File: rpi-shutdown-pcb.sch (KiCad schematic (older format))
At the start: 14 parts

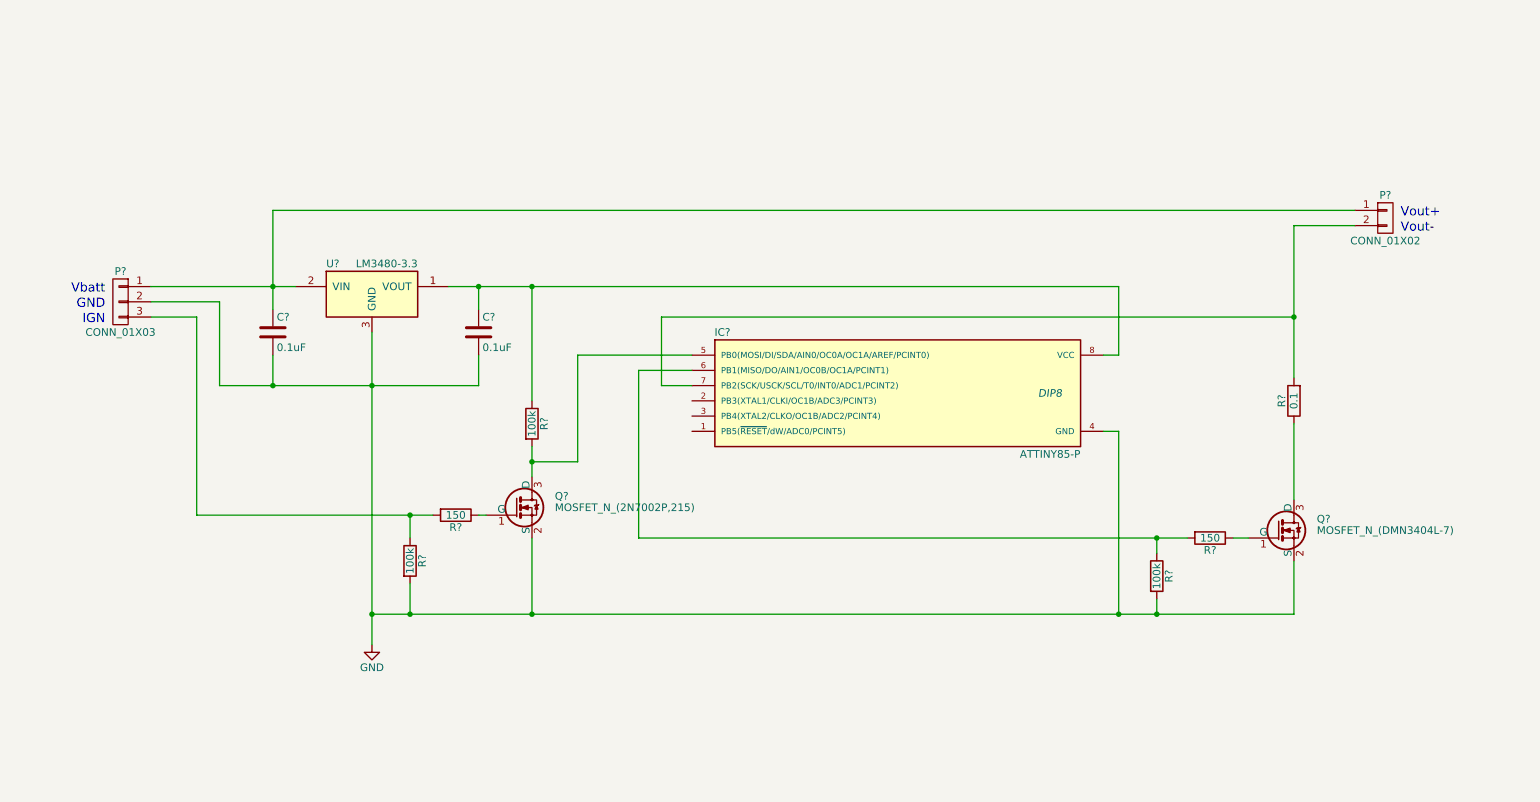
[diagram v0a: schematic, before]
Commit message: finished revised circuit with P-channel FET and footprints
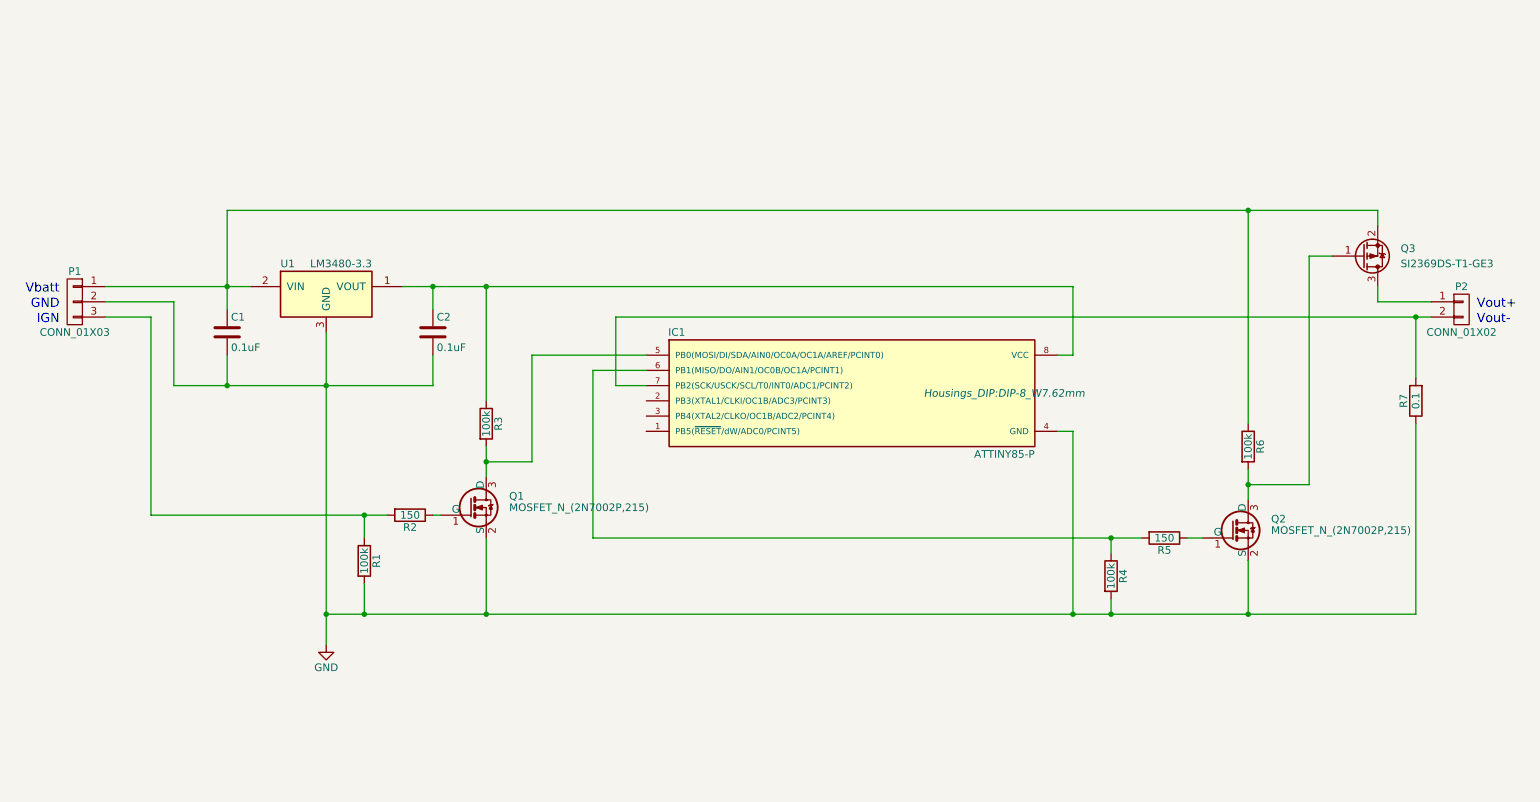
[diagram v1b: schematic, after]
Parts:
- removed Q?: MOSFET_N_(DMN3404L-7), symbol MOSFET_N_(DMN3404L-7)
- added Q2: MOSFET_N_(2N7002P,215), TO_SOT_Packages_SMD:SOT-23_Handsoldering, symbol MOSFET_N_(2N7002P,215)
- added Q3: SI2369DS-T1-GE3, TO_SOT_Packages_SMD:SOT-23_Handsoldering, symbol Q_PMOS_GSD
- added R6: 100k, Resistors_SMD:R_1206_HandSoldering, symbol R
- C1, C2: renamed from C?; footprint (none) -> Capacitors_SMD:C_1206_HandSoldering
- IC1: renamed from IC?; footprint DIP8 -> Housings_DIP:DIP-8_W7.62mm
- P1: renamed from P?; footprint (none) -> rpi-shutdown-pcb:3_PADS_FOR_18_AWG_WIRE
- P2: renamed from P?; footprint (none) -> rpi-shutdown-pcb:2_PADS_FOR_18_AWG_WIRE
- Q1: renamed from Q?; footprint (none) -> TO_SOT_Packages_SMD:SOT-23_Handsoldering
- R1, R2, R3, R4, R5, R7: renamed from R?; footprint (none) -> Resistors_SMD:R_1206_HandSoldering
- U1: renamed from U?; footprint TO_SOT_Packages_SMD:SOT-23 -> TO_SOT_Packages_SMD:SOT-23_Handsoldering
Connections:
- net GND: now also R7.1, Q2.2 (S)
- net at C1.1, P1.1 (P1), U1.2 (VIN): now also Q3.2 (S), R6.1; no longer P2.1 (P1)
- net at R5.1: now also Q2.1 (G)
- new net: P2.1 (P1), Q3.3 (D)
- new net: Q2.3 (D), Q3.1 (G), R6.2
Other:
- moved on the sheet: C1, C2, IC1, P1, P2, Q1, R1, R2, R3, R4, R5, R7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

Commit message: -finished pcb layout.
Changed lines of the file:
@@
 LIBS:valves
 LIBS:rpi-shutdown-pcb
-LIBS:Smart Tank Motherboard-cache
 LIBS:rpi-shutdown-pcb-cache
 EELAYER 25 0
@@
 F 0 "IC1" H 5250 4250 50  0000 C CNN
 F 1 "ATTINY85-P" H 7400 3450 50  0000 C CNN
-F 2 "Housings_DIP:DIP-8_W7.62mm" H 7400 3850 50  0000 C CIN
+F 2 "Housings_DIP:DIP-8_W7.62mm" H 7400 3850 50  0001 C CIN
 F 3 "" H 6400 3850 50  0000 C CNN
 	1    6400 3850

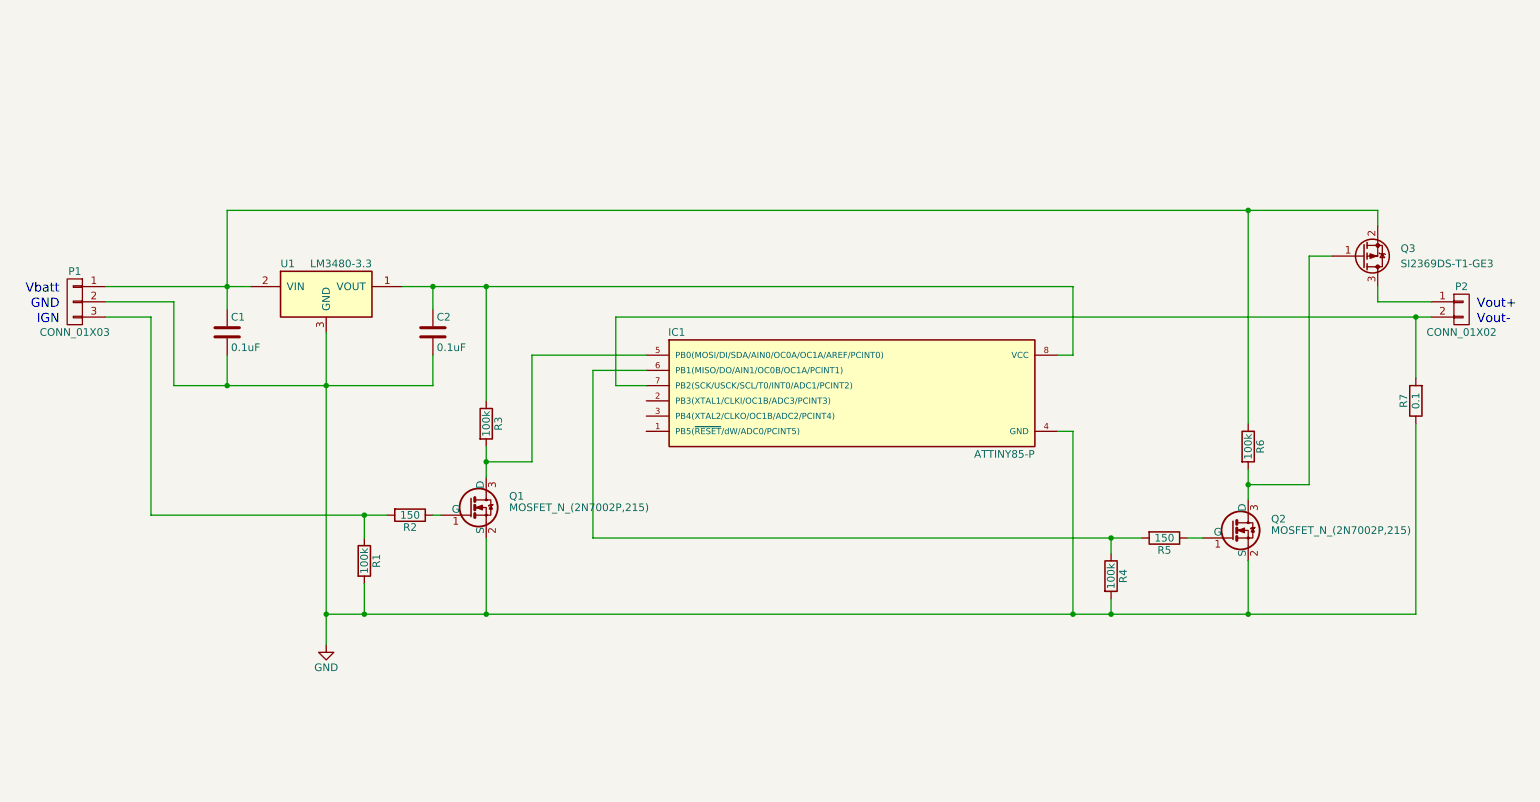
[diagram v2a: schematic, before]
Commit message: Finished adding step-down converter circuit.  Need to start on footprints.
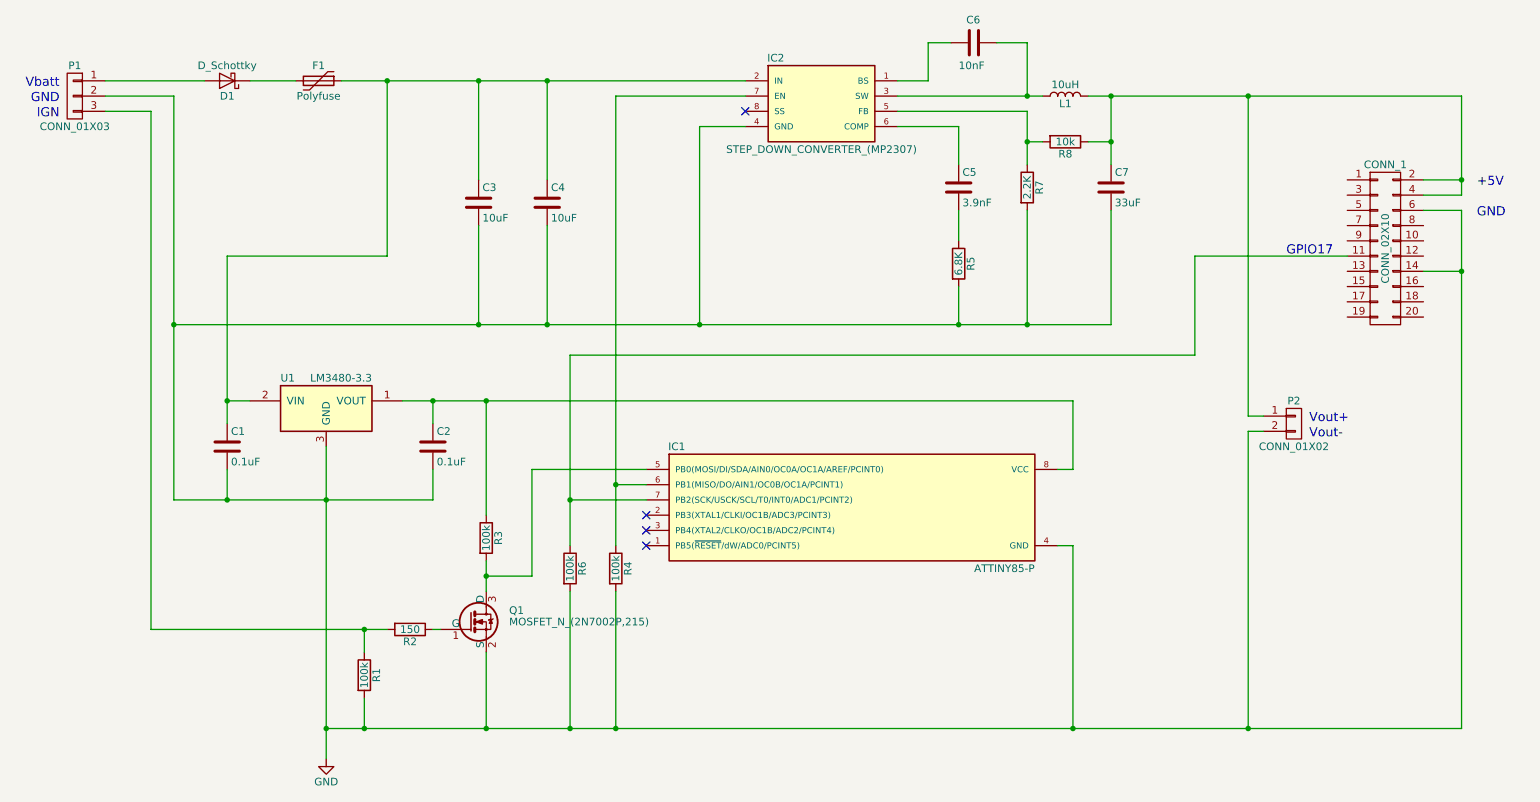
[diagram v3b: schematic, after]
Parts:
- removed Q2: MOSFET_N_(2N7002P,215), TO_SOT_Packages_SMD:SOT-23_Handsoldering, symbol MOSFET_N_(2N7002P,215)
- removed Q3: SI2369DS-T1-GE3, TO_SOT_Packages_SMD:SOT-23_Handsoldering, symbol Q_PMOS_GSD
- added C3, C4: 10uF, Capacitors_SMD:C_1206_HandSoldering, symbol C
- added C5: 3.9nF, Capacitors_SMD:C_1206_HandSoldering, symbol C
- added C6: 10nF, Capacitors_SMD:C_1206_HandSoldering, symbol C
- added C7: 33uF, Capacitors_SMD:C_1206_HandSoldering, symbol C
- added CONN_1: CONN_02X10, symbol CONN_02X10
- added D1: D_Schottky, symbol D_Schottky
- added F1: Polyfuse, symbol Polyfuse
- added IC2: STEP_DOWN_CONVERTER_(MP2307), DIP8, symbol STEP_DOWN_CONVERTER_(MP2307)
- added L1: 10uH, symbol L
- added R8: 10k, Resistors_SMD:R_1206_HandSoldering, symbol R
- P1: footprint rpi-shutdown-pcb:3_PADS_FOR_18_AWG_WIRE -> (none)
- R5: value 150 -> 6.8K
- R7: value 0.1 -> 2.2K
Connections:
- net GND: now also P2.2 (P2), R5.2, R6.2, R7.2, C3.2, C4.2, C7.2, CONN_1.14 (P14), CONN_1.6 (P6), IC2.4 (GND), IC2.9 (GND); no longer R7.1
- net at IC1.6 (PB1(MISO/DO/AIN1/OC0B/OC1A/PCINT1)), R4.1: now also IC2.7 (EN); no longer R5.2
- net at C1.1, U1.2 (VIN): now also C3.1, C4.1, F1.1, IC2.2 (IN); no longer P1.1 (P1), R6.1
- net at P2.1 (P1): now also C7.1, CONN_1.2 (P2), CONN_1.4 (P4), L1.2, R8.1
- net at R5.1: now also C5.2
- new net: CONN_1.11 (P11), IC1.7 (PB2(SCK/USCK/SCL/T0/INT0/ADC1/PCINT2)), R6.1
- new net: C6.2, IC2.1 (BS)
- new net: C6.1, IC2.3 (SW), L1.1
- new net: IC2.5 (FB), R7.1, R8.2
- new net: C5.1, IC2.6 (COMP)
- new net: D1.1 (K), F1.2
- new net: D1.2 (A), P1.1 (P1)
- no-connect marks 0 -> 4
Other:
- note added: "+5V"
- note added: "GPIO17"
- moved on the sheet: C1, C2, IC1, P2, Q1, R1, R2, R3, R6, U1

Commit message: Finished footprints.
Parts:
- C1, C2, C3, C4, C7: footprint Capacitors_SMD:C_1206_HandSoldering -> rpi-shutdown-pcb:R_1206_HandSoldering_(narrow)
- C5, C6: footprint Capacitors_SMD:C_1206_HandSoldering -> rpi-shutdown-pcb:C_0805_HandSoldering_(narrow)
- CONN_1: footprint (none) -> rpi-shutdown-pcb:HEADER_20_PIN_FEMALE_(PPTC102LFBN-RC)
- D1: footprint (none) -> rpi-shutdown-pcb:DO-214AB
- F1: footprint (none) -> rpi-shutdown-pcb:R_1812_HandSoldering
- IC2: footprint DIP8 -> rpi-shutdown-pcb:SOIC8N_(EXPOSED_PAD)
- P1: footprint (none) -> rpi-shutdown-pcb:3_PADS_FOR_18_AWG_WIRE
- R1, R2, R3, R4, R5, R6, R7, R8: footprint Resistors_SMD:R_1206_HandSoldering -> rpi-shutdown-pcb:R_1206_HandSoldering_(narrow)
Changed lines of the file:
@@
 F 0 "C1" H 2325 4300 50  0000 L CNN
 F 1 "0.1uF" H 2325 4100 50  0000 L CNN
-F 2 "Capacitors_SMD:C_1206_HandSoldering" H 2338 4050 50  0001 C CNN
+F 2 "rpi-shutdown-pcb:R_1206_HandSoldering_(narrow)" H 2338 4050 50  0001 C CNN
 F 3 "" H 2300 4200 50  0000 C CNN
 	1    2300 4200
@@
 F 0 "C2" H 3675 4300 50  0000 L CNN
 F 1 "0.1uF" H 3675 4100 50  0000 L CNN
-F 2 "Capacitors_SMD:C_1206_HandSoldering" H 3688 4050 50  0001 C CNN
+F 2 "rpi-shutdown-pcb:R_1206_HandSoldering_(narrow)" H 3688 4050 50  0001 C CNN
 F 3 "" H 3650 4200 50  0000 C CNN
 	1    3650 4200
@@
 F 0 "R2" V 3580 5400 50  0000 C CNN
 F 1 "150" V 3500 5400 50  0000 C CNN
-F 2 "Resistors_SMD:R_1206_HandSoldering" V 3430 5400 50  0001 C CNN
+F 2 "rpi-shutdown-pcb:R_1206_HandSoldering_(narrow)" V 3430 5400 50  0001 C CNN
 F 3 "" H 3500 5400 50  0000 C CNN
 	1    3500 5400
@@
 F 0 "R3" V 4080 4800 50  0000 C CNN
 F 1 "100k" V 4000 4800 50  0000 C CNN
-F 2 "Resistors_SMD:R_1206_HandSoldering" V 3930 4800 50  0001 C CNN
+F 2 "rpi-shutdown-pcb:R_1206_HandSoldering_(narrow)" V 3930 4800 50  0001 C CNN
 F 3 "" H 4000 4800 50  0000 C CNN
 	1    4000 4800
@@
 F 0 "R1" V 3280 5700 50  0000 C CNN
 F 1 "100k" V 3200 5700 50  0000 C CNN
-F 2 "Resistors_SMD:R_1206_HandSoldering" V 3130 5700 50  0001 C CNN
+F 2 "rpi-shutdown-pcb:R_1206_HandSoldering_(narrow)" V 3130 5700 50  0001 C CNN
 F 3 "" H 3200 5700 50  0000 C CNN
 	1    3200 5700
@@
 F 0 "R6" V 4630 5000 50  0000 C CNN
 F 1 "100k" V 4550 5000 50  0000 C CNN
-F 2 "Resistors_SMD:R_1206_HandSoldering" V 4480 5000 50  0001 C CNN
+F 2 "rpi-shutdown-pcb:R_1206_HandSoldering_(narrow)" V 4480 5000 50  0001 C CNN
 F 3 "" H 4550 5000 50  0000 C CNN
 	1    4550 5000
@@
 F 0 "IC2" H 5900 2250 50  0000 C CNN
 F 1 "STEP_DOWN_CONVERTER_(MP2307)" H 6200 1650 50  0000 C CNN
-F 2 "DIP8" H 6200 1550 50  0001 C CIN
+F 2 "rpi-shutdown-pcb:SOIC8N_(EXPOSED_PAD)" H 6200 1550 50  0001 C CIN
 F 3 "" H 6200 1950 50  0000 C CNN
 	1    6200 1950
@@
 F 0 "D1" H 2300 1900 50  0000 C CNN
 F 1 "D_Schottky" H 2300 1700 50  0000 C CNN
-F 2 "" H 2300 1800 50  0001 C CNN
+F 2 "rpi-shutdown-pcb:DO-214AB" H 2300 1800 50  0001 C CNN
 F 3 "" H 2300 1800 50  0001 C CNN
 	1    2300 1800
@@
 F 0 "F1" V 2800 1800 50  0000 C CNN
 F 1 "Polyfuse" V 3000 1800 50  0000 C CNN
-F 2 "" H 2950 1600 50  0001 L CNN
+F 2 "rpi-shutdown-pcb:R_1812_HandSoldering" H 2950 1600 50  0001 L CNN
 F 3 "" H 2900 1800 50  0001 C CNN
 	1    2900 1800
@@
 F 0 "C3" H 3975 2700 50  0000 L CNN
 F 1 "10uF" H 3975 2500 50  0000 L CNN
-F 2 "Capacitors_SMD:C_1206_HandSoldering" H 3988 2450 50  0001 C CNN
+F 2 "rpi-shutdown-pcb:R_1206_HandSoldering_(narrow)" H 3988 2450 50  0001 C CNN
 F 3 "" H 3950 2600 50  0000 C CNN
 	1    3950 2600
@@
 F 0 "C4" H 4425 2700 50  0000 L CNN
 F 1 "10uF" H 4425 2500 50  0000 L CNN
-F 2 "Capacitors_SMD:C_1206_HandSoldering" H 4438 2450 50  0001 C CNN
+F 2 "rpi-shutdown-pcb:R_1206_HandSoldering_(narrow)" H 4438 2450 50  0001 C CNN
 F 3 "" H 4400 2600 50  0000 C CNN
 	1    4400 2600
@@
 F 0 "C6" V 7050 1500 50  0000 L CNN
 F 1 "10nF" V 7350 1450 50  0000 L CNN
-F 2 "Capacitors_SMD:C_1206_HandSoldering" H 7238 1400 50  0001 C CNN
+F 2 "rpi-shutdown-pcb:C_0805_HandSoldering_(narrow)" H 7238 1400 50  0001 C CNN
 F 3 "" H 7200 1550 50  0000 C CNN
 	1    7200 1550
@@
 F 0 "R7" V 7630 2500 50  0000 C CNN
 F 1 "2.2K" V 7550 2500 50  0000 C CNN
-F 2 "Resistors_SMD:R_1206_HandSoldering" V 7480 2500 50  0001 C CNN
+F 2 "rpi-shutdown-pcb:R_1206_HandSoldering_(narrow)" V 7480 2500 50  0001 C CNN
 F 3 "" H 7550 2500 50  0000 C CNN
 	1    7550 2500
@@
 F 0 "R8" V 7880 2200 50  0000 C CNN
 F 1 "10k" V 7800 2200 50  0000 C CNN
-F 2 "Resistors_SMD:R_1206_HandSoldering" V 7730 2200 50  0001 C CNN
+F 2 "rpi-shutdown-pcb:R_1206_HandSoldering_(narrow)" V 7730 2200 50  0001 C CNN
 F 3 "" H 7800 2200 50  0000 C CNN
 	1    7800 2200
@@
 F 0 "C7" H 8125 2600 50  0000 L CNN
 F 1 "33uF" H 8125 2400 50  0000 L CNN
-F 2 "Capacitors_SMD:C_1206_HandSoldering" H 8138 2350 50  0001 C CNN
+F 2 "rpi-shutdown-pcb:R_1206_HandSoldering_(narrow)" H 8138 2350 50  0001 C CNN
 F 3 "" H 8100 2500 50  0000 C CNN
 	1    8100 2500
@@
 F 0 "C5" H 7125 2600 50  0000 L CNN
 F 1 "3.9nF" H 7125 2400 50  0000 L CNN
-F 2 "Capacitors_SMD:C_1206_HandSoldering" H 7138 2350 50  0001 C CNN
+F 2 "rpi-shutdown-pcb:C_0805_HandSoldering_(narrow)" H 7138 2350 50  0001 C CNN
 F 3 "" H 7100 2500 50  0000 C CNN
 	1    7100 2500
@@
 F 0 "R5" V 7180 3000 50  0000 C CNN
 F 1 "6.8K" V 7100 3000 50  0000 C CNN
-F 2 "Resistors_SMD:R_1206_HandSoldering" V 7030 3000 50  0001 C CNN
+F 2 "rpi-shutdown-pcb:R_1206_HandSoldering_(narrow)" V 7030 3000 50  0001 C CNN
 F 3 "" H 7100 3000 50  0000 C CNN
 	1    7100 3000
@@
 F 0 "R4" V 4930 5000 50  0000 C CNN
 F 1 "100k" V 4850 5000 50  0000 C CNN
-F 2 "Resistors_SMD:R_1206_HandSoldering" V 4780 5000 50  0001 C CNN
+F 2 "rpi-shutdown-pcb:R_1206_HandSoldering_(narrow)" V 4780 5000 50  0001 C CNN
 F 3 "" H 4850 5000 50  0000 C CNN
 	1    4850 5000
@@
 F 0 "P1" H 1300 2100 50  0000 C CNN
 F 1 "CONN_01X03" H 1300 1700 50  0000 C CNN
-F 2 "" H 1300 1900 50  0001 C CNN
+F 2 "rpi-shutdown-pcb:3_PADS_FOR_18_AWG_WIRE" H 1300 1900 50  0001 C CNN
 F 3 "" H 1300 1900 50  0001 C CNN
 	1    1300 1900
@@
 F 0 "CONN_1" H 9900 3450 50  0000 C CNN
 F 1 "CONN_02X10" V 9900 2900 50  0000 C CNN
-F 2 "" H 9900 1700 50  0001 C CNN
+F 2 "rpi-shutdown-pcb:HEADER_20_PIN_FEMALE_(PPTC102LFBN-RC)" H 9900 1700 50  0001 C CNN
 F 3 "" H 9900 1700 50  0001 C CNN
 	1    9900 2900

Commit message: Finished PCB layout.  Ready to try routing.
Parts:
- L1: footprint (none) -> rpi-shutdown-pcb:INDUCTOR_10uH_(ASPI-0630LR)
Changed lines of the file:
@@
 LIBS:valves
 LIBS:rpi-shutdown-pcb
-LIBS:Smart Tank Motherboard-cache
 LIBS:rpi-shutdown-pcb-cache
 EELAYER 25 0
@@
 F 0 "L1" V 7750 1900 50  0000 C CNN
 F 1 "10uH" V 7875 1900 50  0000 C CNN
-F 2 "" H 7800 1900 50  0001 C CNN
+F 2 "rpi-shutdown-pcb:INDUCTOR_10uH_(ASPI-0630LR)" H 7800 1900 50  0001 C CNN
 F 3 "" H 7800 1900 50  0001 C CNN
 	1    7800 1900
